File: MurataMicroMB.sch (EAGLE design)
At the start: 47 parts, among them CON1 C-2395.MurataMicroSD, CON3 CON_MIL_10_ARM, CON4 C-2395.microSD, IC1 74LVC1G00DBV, IC2 IC_DCDC_LM27313, IC3 IC_LPC11U3XQFN33, IC4 IC_LDO_XX1117_4, Q1 CLOCK_CRYSTAL_4_3225, SW1 SW_TACTSW_2PP8073, SW2 SW_TACTSW_2PP8073, SW3 SW_TACTSW_2PP8073, X1 TSW-102-02-S-S

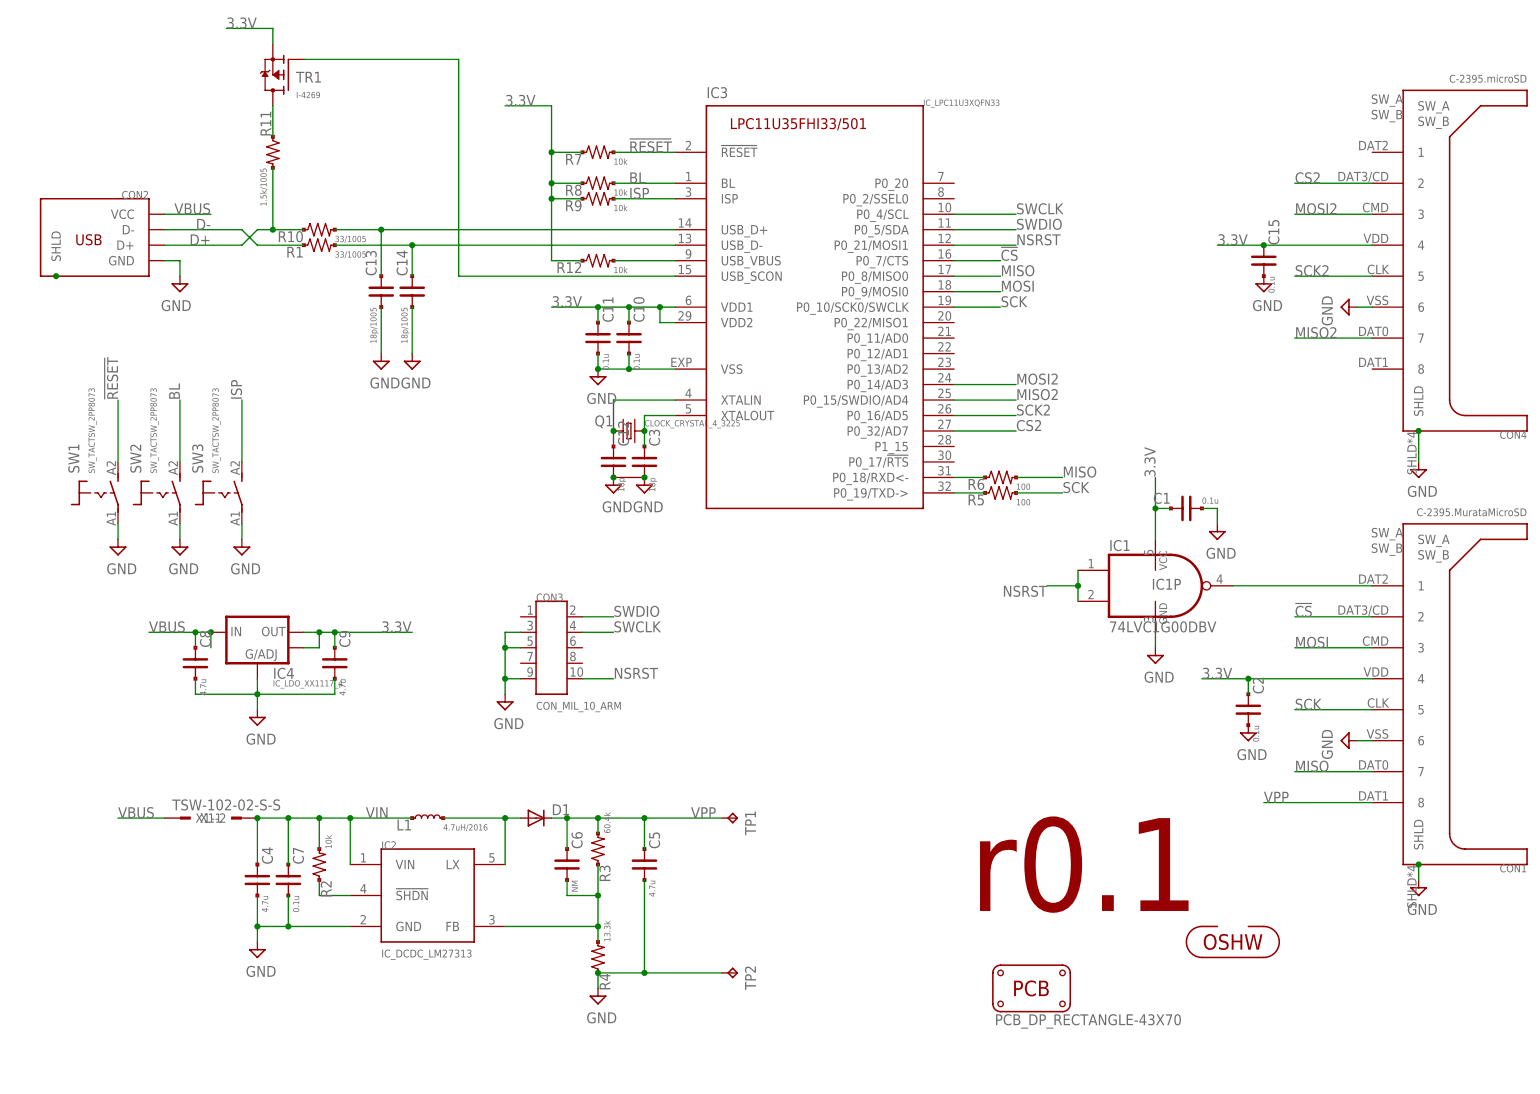
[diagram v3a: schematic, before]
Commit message: [ MB ][ SCH ] connection to uSD sockets changed
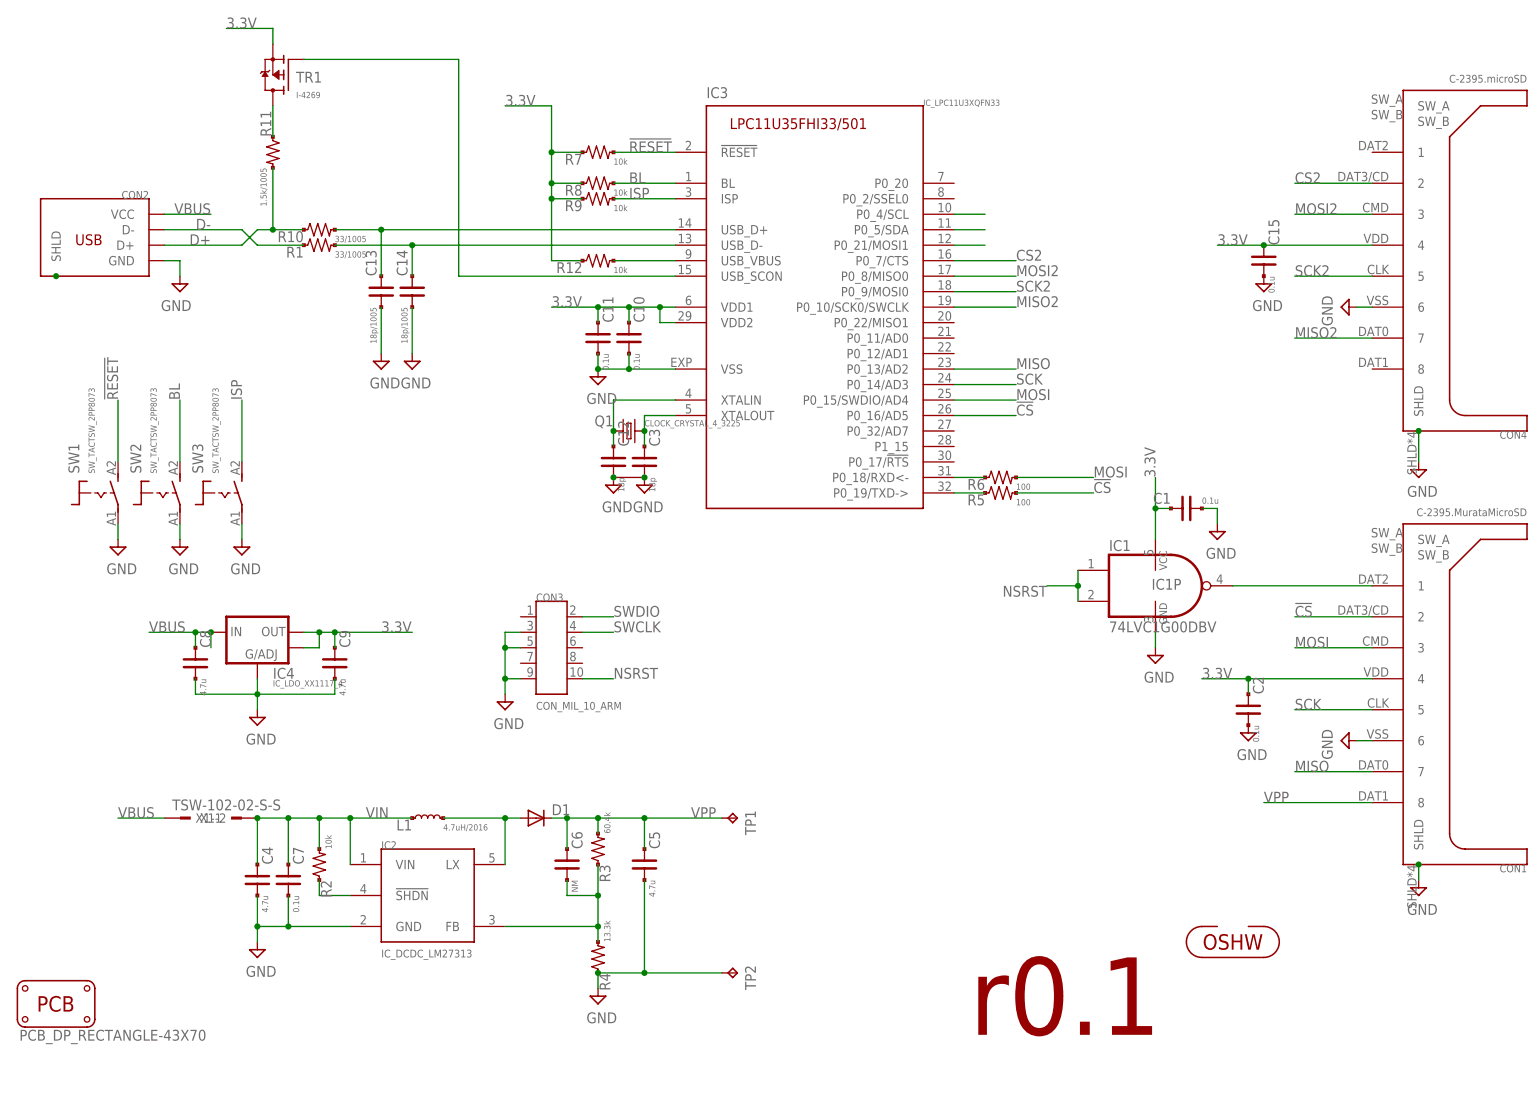
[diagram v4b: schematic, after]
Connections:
- net !CS!: now also IC3.P0_16/AD5, R5.2; no longer IC3.P0_7/CTS
- net CS2: now also IC3.P0_7/CTS; no longer IC3.P0_32/AD7
- net MISO: now also IC3.P0_13/AD2; no longer IC3.P0_8/MISO0, R6.2
- net MISO2: now also IC3.P0_10/SCK0/SWCLK; no longer IC3.P0_15/SWDIO/AD4
- net MOSI: now also IC3.P0_15/SWDIO/AD4, R6.2; no longer IC3.P0_9/MOSI0
- net MOSI2: now also IC3.P0_8/MISO0; no longer IC3.P0_14/AD3
- net SCK: now also IC3.P0_14/AD3; no longer IC3.P0_10/SCK0/SWCLK, R5.2
- net SCK2: now also IC3.P0_9/MOSI0; no longer IC3.P0_16/AD5
- net SWCLK: now also IC3.P0_5/SDA; no longer IC3.P0_4/SCL
- net SWDIO: now also IC3.P0_4/SCL; no longer IC3.P0_5/SDA
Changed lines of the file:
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@@
 <sheet>
 <plain>
-<text x="162.56" y="25.4" size="15.24" layer="94">r0.1</text>
+<text x="162.56" y="5.08" size="12.7" layer="94">r0.1</text>
 </plain>
 <instances>
 <instance part="FRAME1" gate="G$1" x="0" y="0"/>
 <instance part="CON1" gate="G$1" x="241.3" y="60.96"/>
-<instance part="PCB1" gate="G$1" x="172.72" y="12.7"/>
+<instance part="PCB1" gate="G$1" x="12.7" y="10.16"/>
 <instance part="IC1" gate="A" x="193.04" y="78.74"/>
 <instance part="IC1" gate="P" x="193.04" y="78.74"/>
@@
 </segment>
 <segment>
-<wire x1="160.02" y1="139.7" x2="170.18" y2="139.7" width="0.1524" layer="91"/>
-<label x="170.18" y="139.7" size="1.778" layer="95"/>
-<pinref part="IC3" gate="G$1" pin="P0_4/SCL"/>
+<wire x1="160.02" y1="137.16" x2="165.1" y2="137.16" width="0.1524" layer="91"/>
+<pinref part="IC3" gate="G$1" pin="P0_5/SDA"/>
 </segment>
 </net>
@@
 </segment>
 <segment>
-<wire x1="160.02" y1="137.16" x2="170.18" y2="137.16" width="0.1524" layer="91"/>
-<label x="170.18" y="137.16" size="1.778" layer="95"/>
-<pinref part="IC3" gate="G$1" pin="P0_5/SDA"/>
+<wire x1="160.02" y1="139.7" x2="165.1" y2="139.7" width="0.1524" layer="91"/>
+<pinref part="IC3" gate="G$1" pin="P0_4/SCL"/>
 </segment>
 </net>
@@
 </segment>
 <segment>
-<wire x1="160.02" y1="134.62" x2="170.18" y2="134.62" width="0.1524" layer="91"/>
-<label x="170.18" y="134.62" size="1.778" layer="95"/>
+<wire x1="160.02" y1="134.62" x2="165.1" y2="134.62" width="0.1524" layer="91"/>
 <pinref part="IC3" gate="G$1" pin="P0_21/MOSI1"/>
 </segment>
@@
 </segment>
 <segment>
-<wire x1="167.64" y1="124.46" x2="160.02" y2="124.46" width="0.1524" layer="91"/>
-<pinref part="IC3" gate="G$1" pin="P0_10/SCK0/SWCLK"/>
-<label x="167.64" y="124.46" size="1.778" layer="95"/>
-</segment>
-<segment>
-<wire x1="177.8" y1="93.98" x2="170.18" y2="93.98" width="0.1524" layer="91"/>
-<label x="177.8" y="93.98" size="1.778" layer="95"/>
-<pinref part="R5" gate="G$1" pin="2"/>
+<wire x1="170.18" y1="111.76" x2="160.02" y2="111.76" width="0.1524" layer="91"/>
+<pinref part="IC3" gate="G$1" pin="P0_14/AD3"/>
+<label x="170.18" y="111.76" size="1.778" layer="95"/>
 </segment>
 </net>
@@
 </segment>
 <segment>
-<wire x1="167.64" y1="129.54" x2="160.02" y2="129.54" width="0.1524" layer="91"/>
-<pinref part="IC3" gate="G$1" pin="P0_8/MISO0"/>
-<label x="167.64" y="129.54" size="1.778" layer="95"/>
-</segment>
-<segment>
-<wire x1="177.8" y1="96.52" x2="170.18" y2="96.52" width="0.1524" layer="91"/>
-<label x="177.8" y="96.52" size="1.778" layer="95"/>
-<pinref part="R6" gate="G$1" pin="2"/>
+<wire x1="170.18" y1="114.3" x2="160.02" y2="114.3" width="0.1524" layer="91"/>
+<pinref part="IC3" gate="G$1" pin="P0_13/AD2"/>
+<label x="170.18" y="114.3" size="1.778" layer="95"/>
 </segment>
 </net>
@@
 </segment>
 <segment>
-<wire x1="167.64" y1="127" x2="160.02" y2="127" width="0.1524" layer="91"/>
-<pinref part="IC3" gate="G$1" pin="P0_9/MOSI0"/>
-<label x="167.64" y="127" size="1.778" layer="95"/>
+<wire x1="182.88" y1="96.52" x2="170.18" y2="96.52" width="0.1524" layer="91"/>
+<pinref part="R6" gate="G$1" pin="2"/>
+<label x="182.88" y="96.52" size="1.778" layer="95"/>
+</segment>
+<segment>
+<wire x1="170.18" y1="109.22" x2="160.02" y2="109.22" width="0.1524" layer="91"/>
+<pinref part="IC3" gate="G$1" pin="P0_15/SWDIO/AD4"/>
+<label x="170.18" y="109.22" size="1.778" layer="95"/>
 </segment>
 </net>
@@
 </segment>
 <segment>
-<wire x1="167.64" y1="132.08" x2="160.02" y2="132.08" width="0.1524" layer="91"/>
-<pinref part="IC3" gate="G$1" pin="P0_7/CTS"/>
-<label x="167.64" y="132.08" size="1.778" layer="95"/>
+<wire x1="182.88" y1="93.98" x2="170.18" y2="93.98" width="0.1524" layer="91"/>
+<pinref part="R5" gate="G$1" pin="2"/>
+<label x="182.88" y="93.98" size="1.778" layer="95"/>
+</segment>
+<segment>
+<wire x1="170.18" y1="106.68" x2="160.02" y2="106.68" width="0.1524" layer="91"/>
+<pinref part="IC3" gate="G$1" pin="P0_16/AD5"/>
+<label x="170.18" y="106.68" size="1.778" layer="95"/>
 </segment>
 </net>
@@
 <net name="MOSI2" class="0">
 <segment>
-<pinref part="IC3" gate="G$1" pin="P0_14/AD3"/>
-<wire x1="160.02" y1="111.76" x2="170.18" y2="111.76" width="0.1524" layer="91"/>
-<label x="170.18" y="111.76" size="1.778" layer="95"/>
-</segment>
-<segment>
 <wire x1="215.9" y1="139.7" x2="228.6" y2="139.7" width="0.1524" layer="91"/>
 <label x="215.9" y="139.7" size="1.778" layer="95"/>
 <pinref part="CON4" gate="G$1" pin="3"/>
 </segment>
+<segment>
+<wire x1="160.02" y1="129.54" x2="170.18" y2="129.54" width="0.1524" layer="91"/>
+<pinref part="IC3" gate="G$1" pin="P0_8/MISO0"/>
+<label x="170.18" y="129.54" size="1.778" layer="95"/>
+</segment>
 </net>
 <net name="MISO2" class="0">
-<segment>
-<pinref part="IC3" gate="G$1" pin="P0_15/SWDIO/AD4"/>
-<wire x1="160.02" y1="109.22" x2="170.18" y2="109.22" width="0.1524" layer="91"/>
-<label x="170.18" y="109.22" size="1.778" layer="95"/>
-</segment>
 <segment>
 <wire x1="215.9" y1="119.38" x2="228.6" y2="119.38" width="0.1524" layer="91"/>
@@
 <pinref part="CON4" gate="G$1" pin="7"/>
 </segment>
+<segment>
+<wire x1="160.02" y1="124.46" x2="170.18" y2="124.46" width="0.1524" layer="91"/>
+<pinref part="IC3" gate="G$1" pin="P0_10/SCK0/SWCLK"/>
+<label x="170.18" y="124.46" size="1.778" layer="95"/>
+</segment>
 </net>
 <net name="SCK2" class="0">
-<segment>
-<pinref part="IC3" gate="G$1" pin="P0_16/AD5"/>
-<wire x1="160.02" y1="106.68" x2="170.18" y2="106.68" width="0.1524" layer="91"/>
-<label x="170.18" y="106.68" size="1.778" layer="95"/>
-</segment>
 <segment>
 <wire x1="215.9" y1="129.54" x2="228.6" y2="129.54" width="0.1524" layer="91"/>
@@
 <pinref part="CON4" gate="G$1" pin="5"/>
 </segment>
+<segment>
+<wire x1="160.02" y1="127" x2="170.18" y2="127" width="0.1524" layer="91"/>
+<pinref part="IC3" gate="G$1" pin="P0_9/MOSI0"/>
+<label x="170.18" y="127" size="1.778" layer="95"/>
+</segment>
 </net>
 <net name="CS2" class="0">
-<segment>
-<pinref part="IC3" gate="G$1" pin="P0_32/AD7"/>
-<wire x1="160.02" y1="104.14" x2="170.18" y2="104.14" width="0.1524" layer="91"/>
-<label x="170.18" y="104.14" size="1.778" layer="95"/>
-</segment>
 <segment>
 <wire x1="215.9" y1="144.78" x2="228.6" y2="144.78" width="0.1524" layer="91"/>
@@
 <pinref part="CON4" gate="G$1" pin="2"/>
 </segment>
-</net>
+<segment>
+<wire x1="160.02" y1="132.08" x2="170.18" y2="132.08" width="0.1524" layer="91"/>
+<pinref part="IC3" gate="G$1" pin="P0_7/CTS"/>
+<label x="170.18" y="132.08" size="1.778" layer="95"/>
+</segment>
+</net>

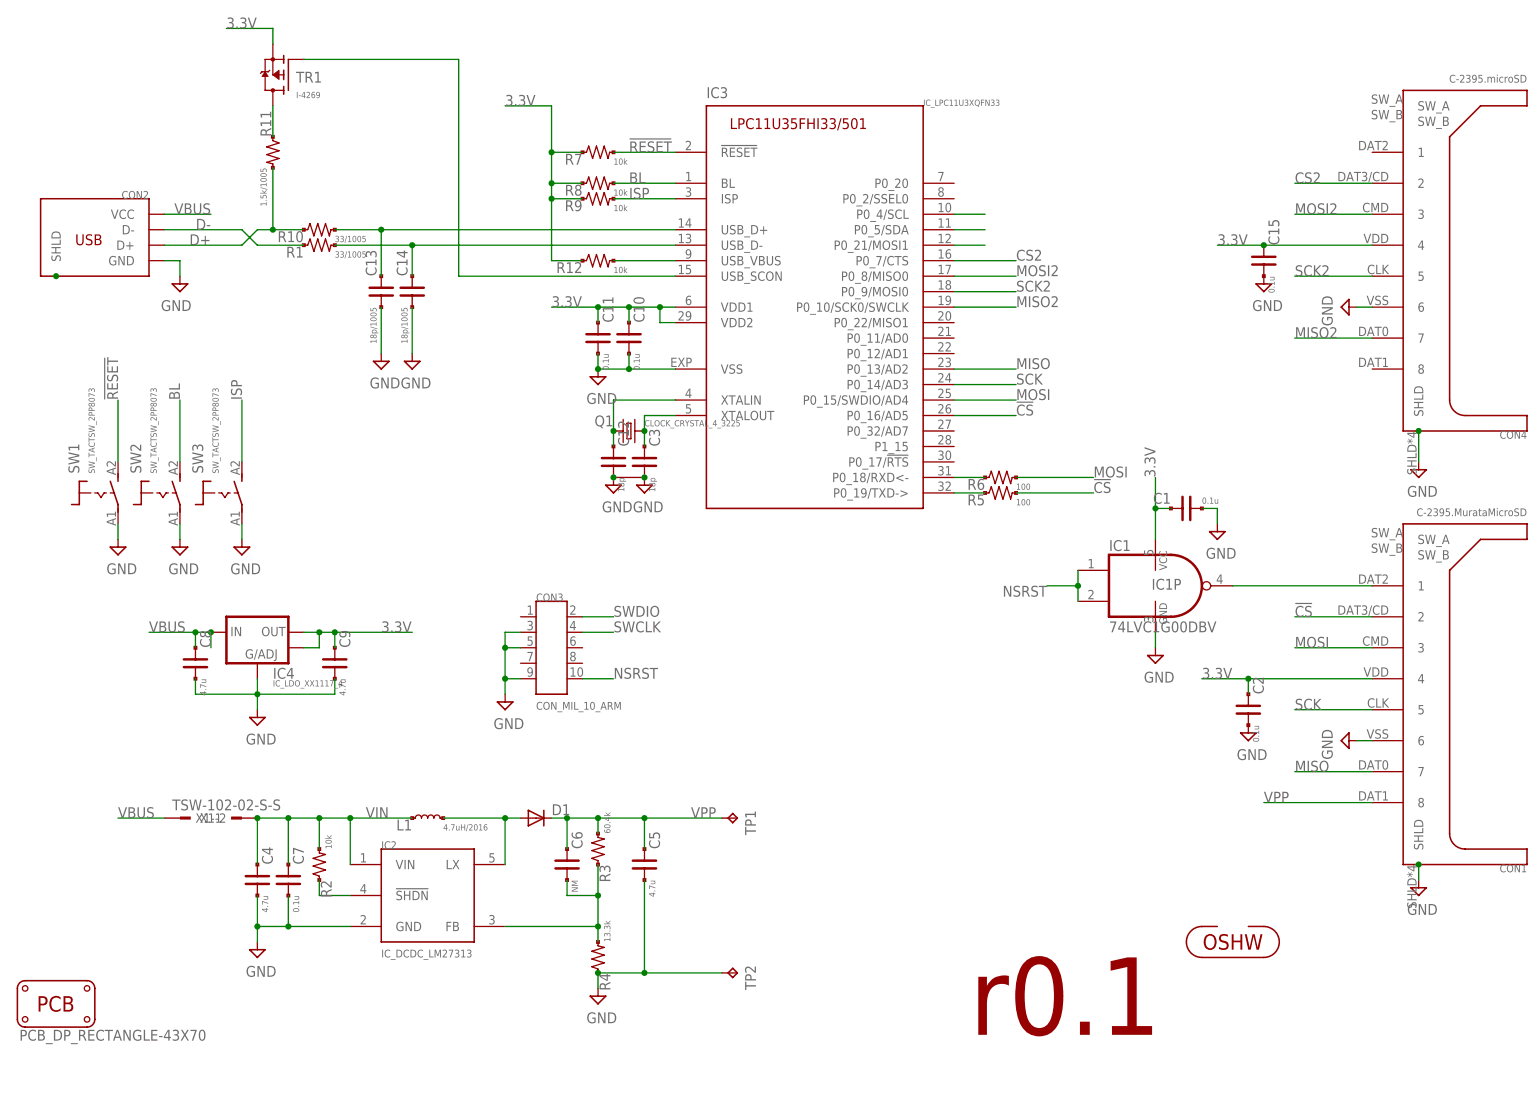
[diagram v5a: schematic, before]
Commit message: [ MB ] RCL value and size
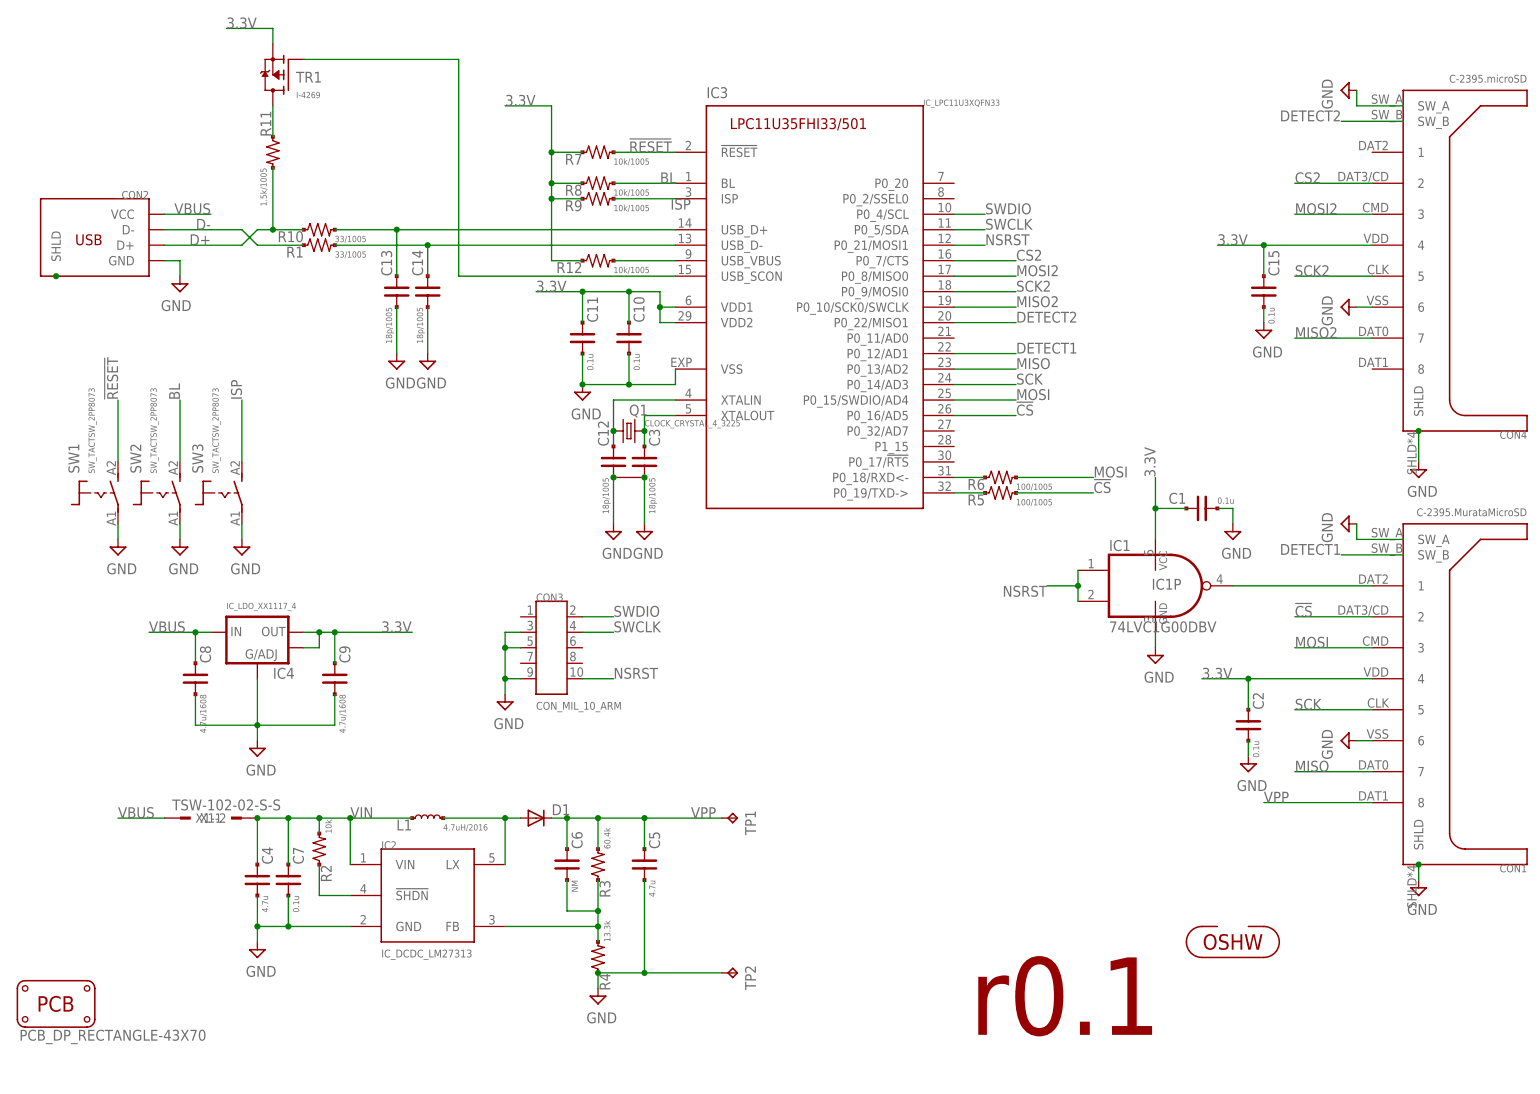
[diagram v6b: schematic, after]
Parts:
- C12, C3: value 18p -> 18p/1005
- C8, C9: value 4.7u -> 4.7u/1608
- R12, R7, R8, R9: value 10k -> 10k/1005
- R5, R6: value 100 -> 100/1005
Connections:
- new net DETECT1: CON1.SW_B, IC3.P0_12/AD1
- new net DETECT2: CON4.SW_B, IC3.P0_22/MISO1
- net GND: now also CON1.SW_A, CON4.SW_A
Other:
- moved on the sheet: C1, C11, C13, C14, C15, C2, C8, C9, R2, R3
